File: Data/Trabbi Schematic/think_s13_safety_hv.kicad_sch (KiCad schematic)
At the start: 5 parts, among them U1 Collision Control Unit (C050), U2 Contactor Box Internal Detail, U3 HV Distribution Box Detail

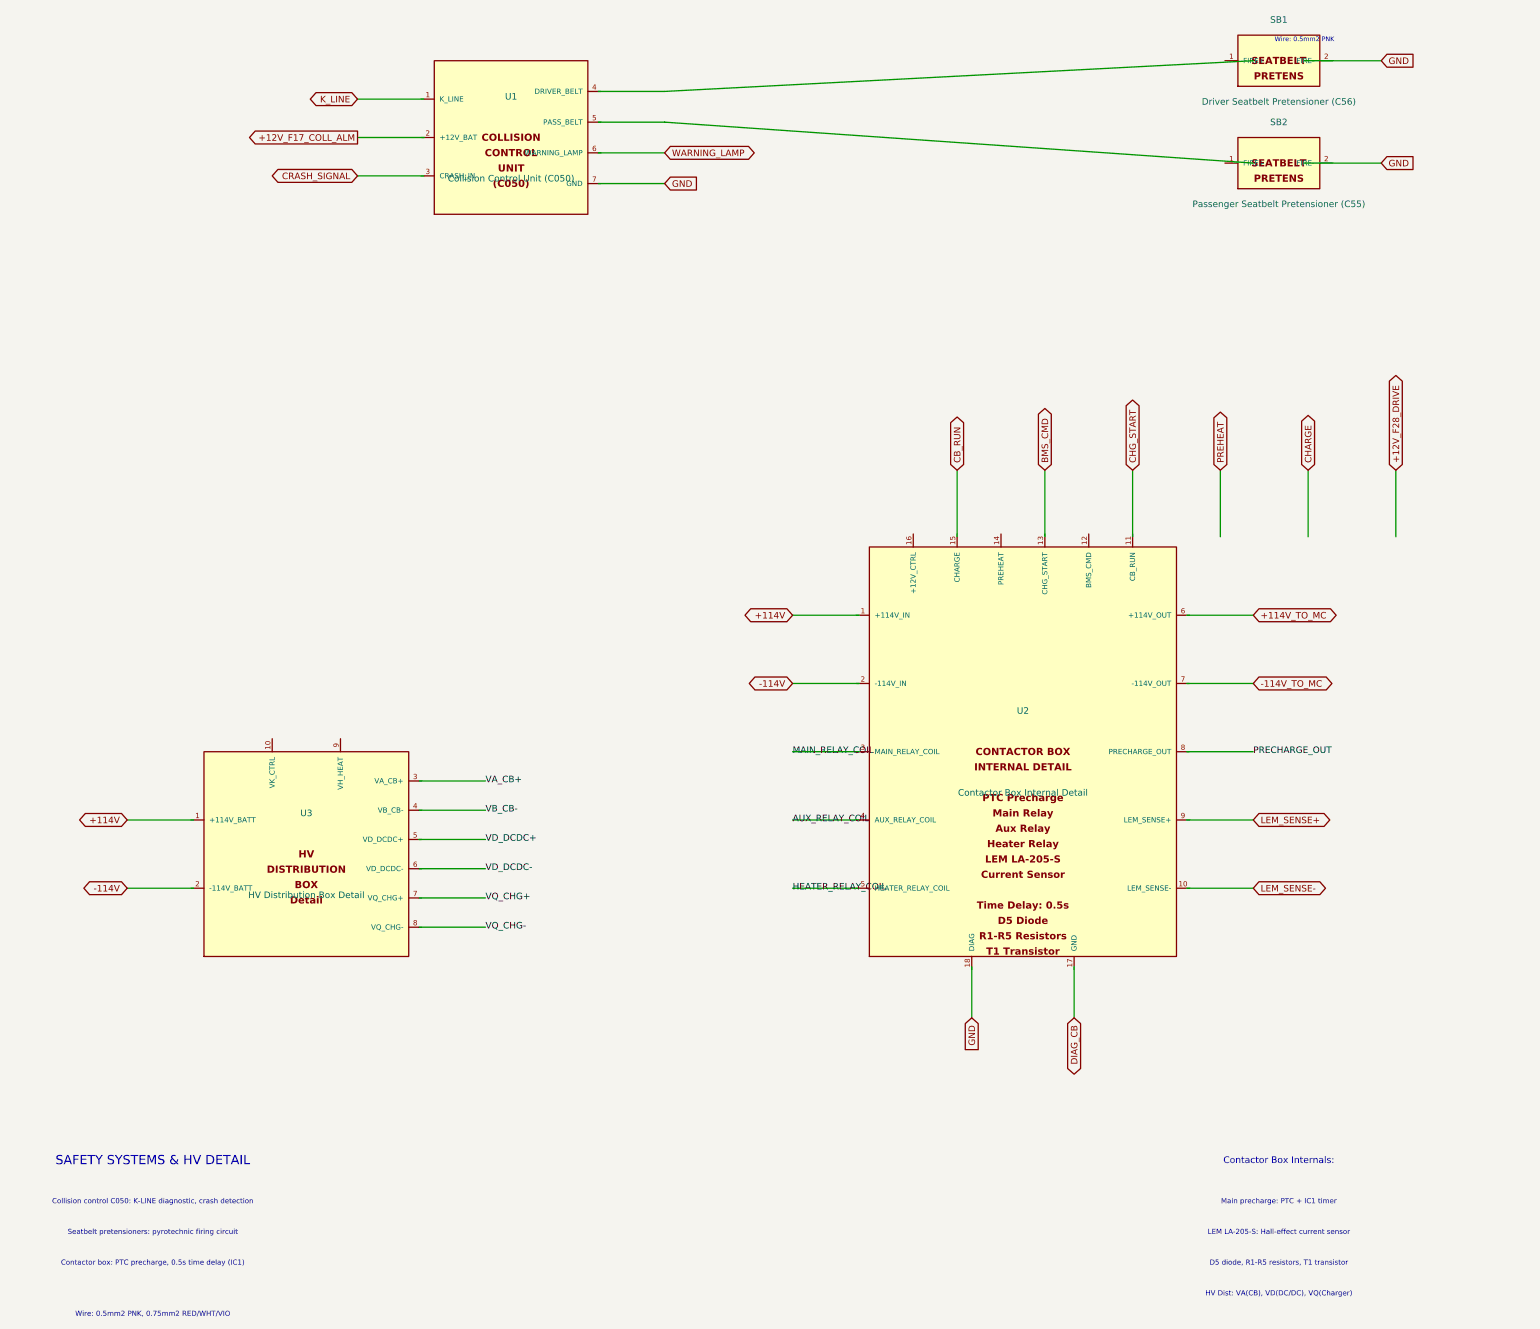
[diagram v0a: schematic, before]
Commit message: Fix wire-to-pin connections: use exact calculated pin positions
Refactored gen_think_complete.py to compute exact pin schematic
coordinates instead of using approximate manual offsets. Added p()
method to Sheet class that transforms symbol-local pin positions to
schematic coordinates. All 232 wire calls across 13 sub-sheet
generators now use p() for pin endpoints, fixing misaligned
connections (previously off by 0.54-10+ units).

Co-Authored-By: Claude Opus 4.6 <noreply@anthropic.com>
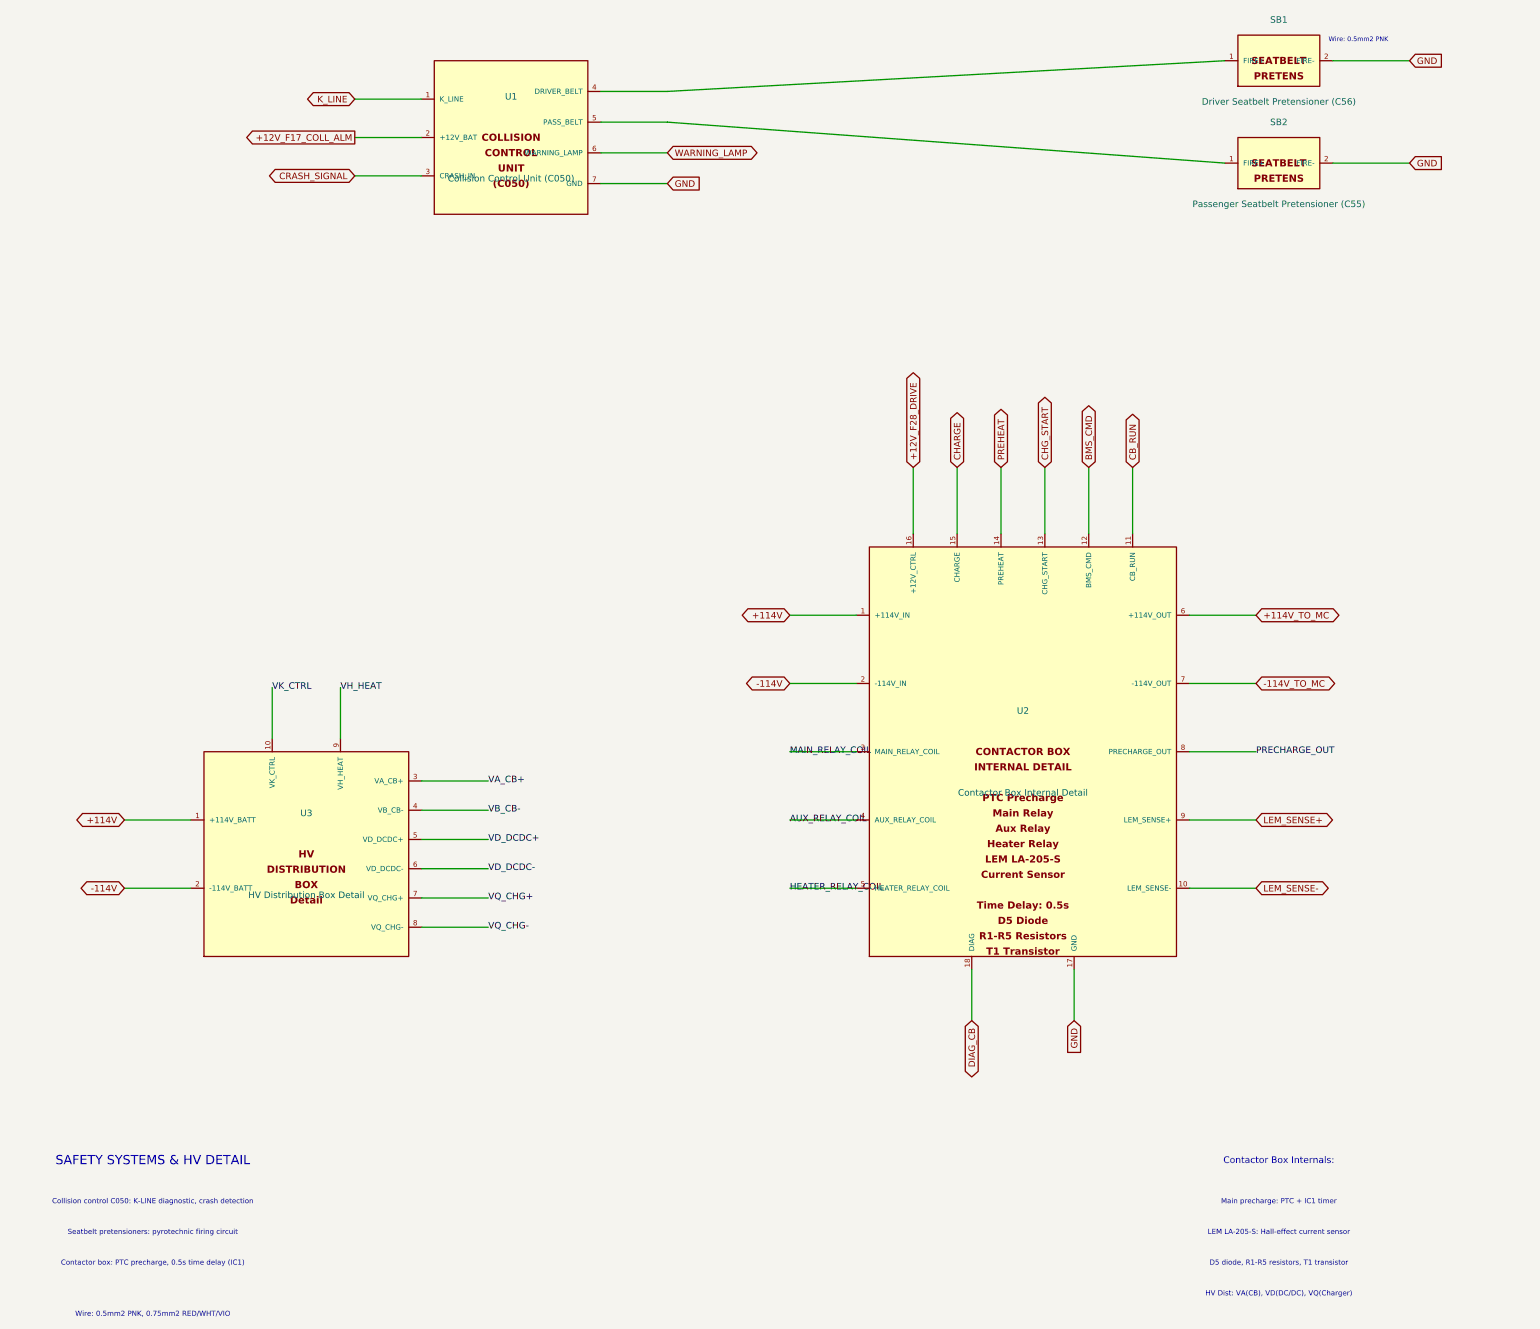
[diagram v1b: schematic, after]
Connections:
- net +114V: now also U2.1 (+114V_IN), U3.1 (+114V_BATT)
- net +114V_TO_MC: now also U2.6 (+114V_OUT)
- net +12V_F17_COLL_ALM: now also U1.2 (+12V_BAT)
- net +12V_F28_DRIVE: now also U2.16 (+12V_CTRL)
- net -114V: now also U2.2 (-114V_IN), U3.2 (-114V_BATT)
- net -114V_TO_MC: now also U2.7 (-114V_OUT)
- net AUX_RELAY_COIL: now also U2.4 (AUX_RELAY_COIL)
- net BMS_CMD: now also U2.12 (BMS_CMD)
- net CB_RUN: now also U2.11 (CB_RUN)
- net CHARGE: now also U2.15 (CHARGE)
- net CHG_START: now also U2.13 (CHG_START)
- net CRASH_SIGNAL: now also U1.3 (CRASH_IN)
- net DIAG_CB: now also U2.18 (DIAG)
- net GND: now also SB1.2 (FIRE-), SB2.2 (FIRE-), U1.7 (GND), U2.17 (GND)
- net HEATER_RELAY_COIL: now also U2.5 (HEATER_RELAY_COIL)
- net K_LINE: now also U1.1 (K_LINE)
- net LEM_SENSE+: now also U2.9 (LEM_SENSE+)
- net LEM_SENSE-: now also U2.10 (LEM_SENSE-)
- net MAIN_RELAY_COIL: now also U2.3 (MAIN_RELAY_COIL)
- net PRECHARGE_OUT: now also U2.8 (PRECHARGE_OUT)
- net PREHEAT: now also U2.14 (PREHEAT)
- net VA_CB+: now also U3.3 (VA_CB+)
- net VB_CB-: now also U3.4 (VB_CB-)
- net VD_DCDC+: now also U3.5 (VD_DCDC+)
- net VD_DCDC-: now also U3.6 (VD_DCDC-)
- net VQ_CHG+: now also U3.7 (VQ_CHG+)
- net VQ_CHG-: now also U3.8 (VQ_CHG-)
- net WARNING_LAMP: now also U1.6 (WARNING_LAMP)
- net VK_CTRL: now reaches U3.10 (VK_CTRL)
- net VH_HEAT: now reaches U3.9 (VH_HEAT)
- net at SB1.1 (FIRE+): now also U1.4 (DRIVER_BELT)
- net at U1.5 (PASS_BELT): now also SB2.1 (FIRE+)

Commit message: Enforce orthogonal routing and 1.27mm grid alignment
- Add _g() grid snap function to Sheet class (rounds all coordinates to nearest 1.27mm)
- Add wire_l() method for L-shaped orthogonal routing (horizontal+vertical segments)
- Apply grid snapping in p(), place(), wire(), label(), glabel(), junction(), no_connect(), defsym()
- Replace all 19 diagonal wire calls with wire_l() across S02, S06, S07, S08, S10, S12, S13
- All wire segments now strictly horizontal or vertical, no diagonals
- All coordinates verified on 1.27mm (50mil) KiCad standard grid

Co-Authored-By: Claude Opus 4.6 <noreply@anthropic.com>
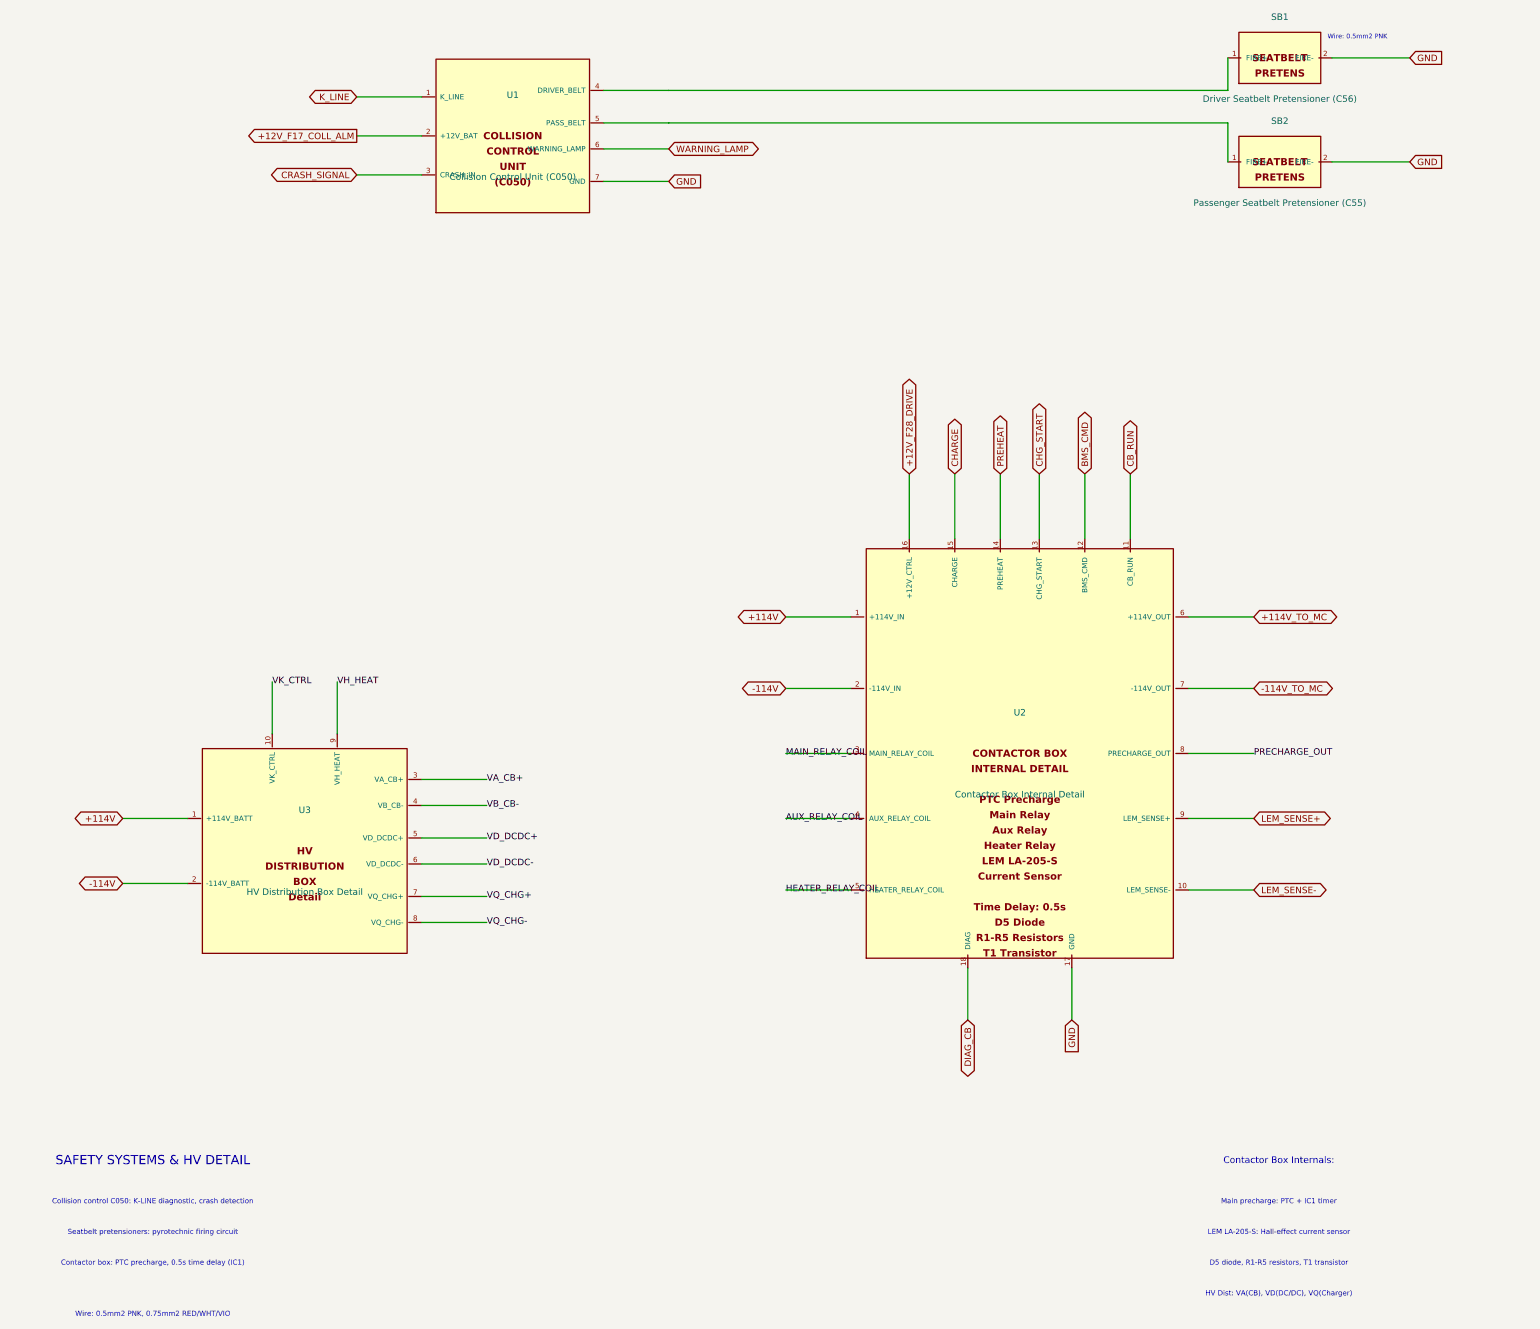
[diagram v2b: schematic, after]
